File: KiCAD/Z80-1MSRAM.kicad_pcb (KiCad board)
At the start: 2 copper layers, 99.1 x 74.9 mm, 23 parts, among them J1 SBC8080 BUS, U1 7402, U2 74HC573, U3 74HC139, U4 74HC04, U5 74HC00, U6 628128, U7 28C256

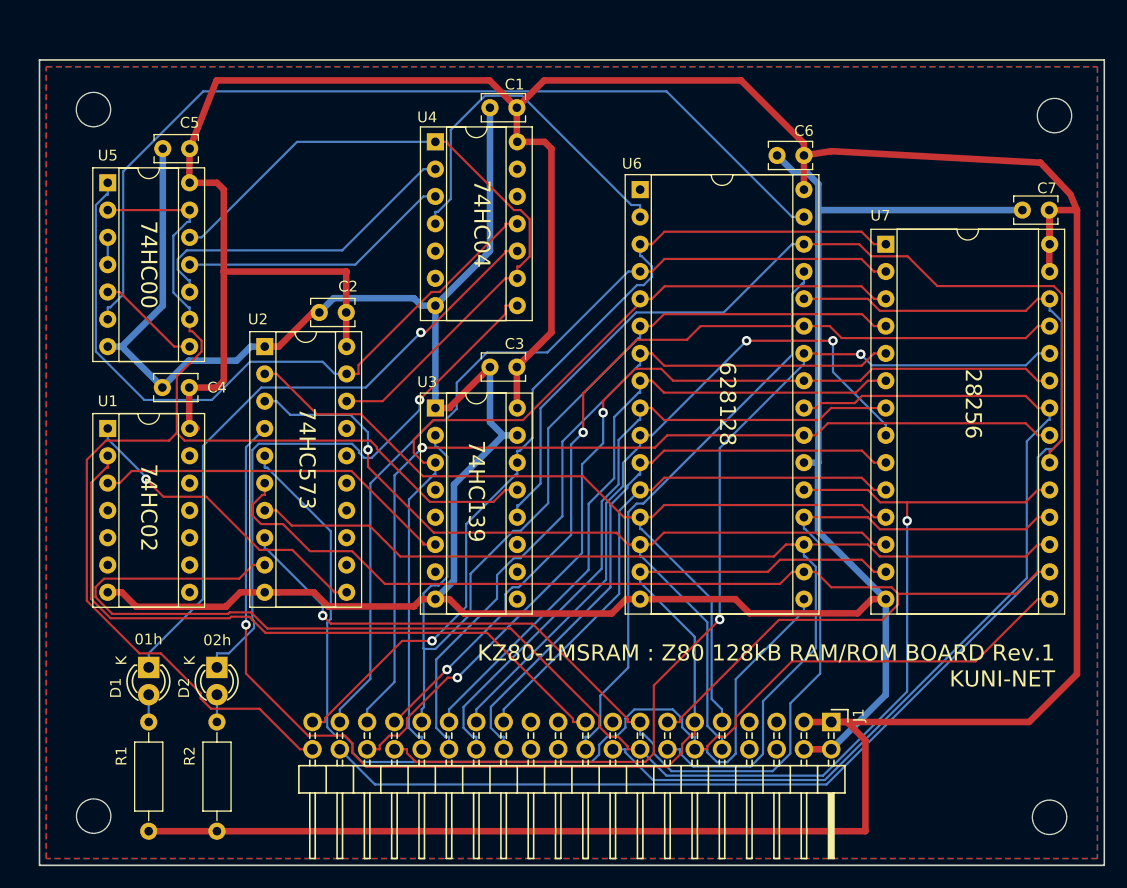
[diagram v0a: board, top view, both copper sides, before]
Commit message: 電源部へコンデンサ追加&パターン調整
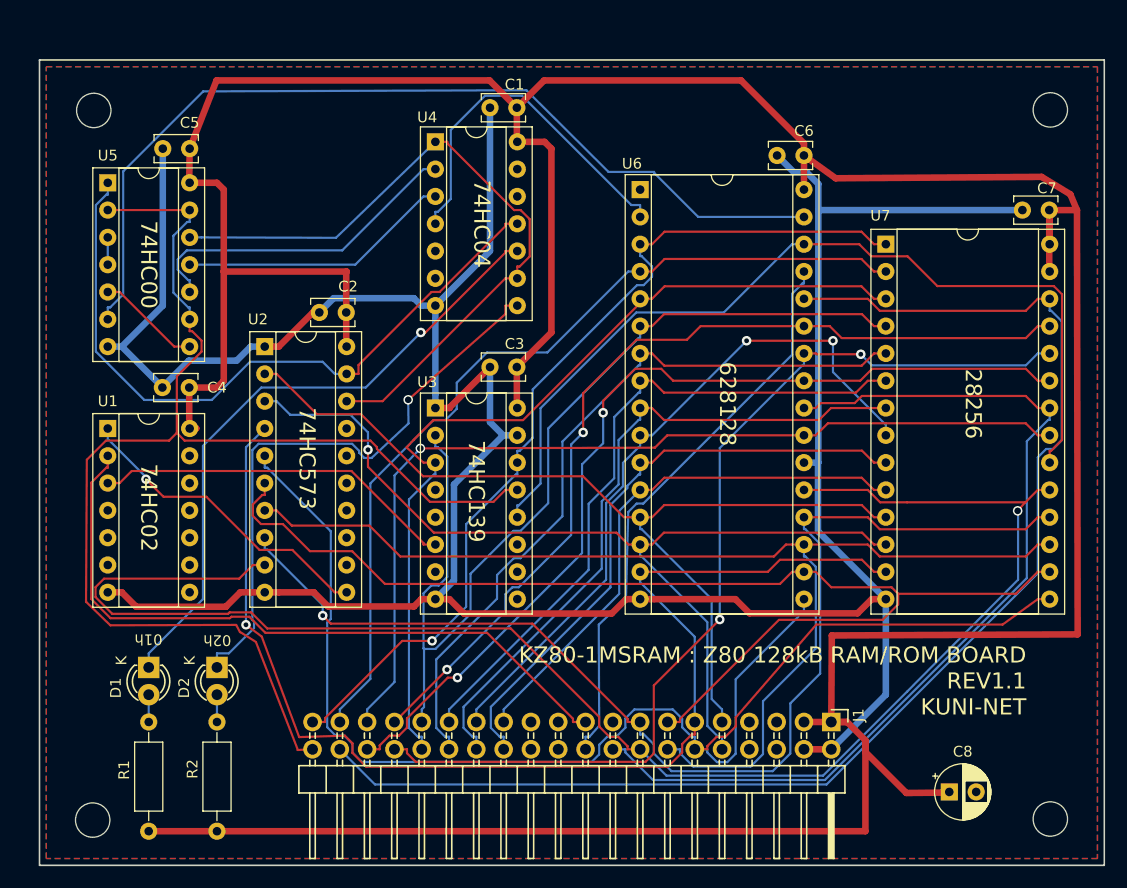
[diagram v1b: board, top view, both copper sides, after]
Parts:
- removed REF** (x4): MountingHole_3.2mm_M3, Mounting_Holes:MountingHole_3.2mm_M3
- added C8: 10u, Capacitor_THT:CP_Radial_D5.0mm_P2.50mm, F.Cu at (186.2, 131.6)
- added MH1: MountingHole, MountingHole:MountingHole_3.2mm_M3, F.Cu at (106.7, 68.2)
- added MH2: MountingHole, MountingHole:MountingHole_3.2mm_M3, F.Cu at (195.6, 68.2)
- added MH3: MountingHole, MountingHole:MountingHole_3.2mm_M3, F.Cu at (106.5, 134.2)
- added MH4: MountingHole, MountingHole:MountingHole_3.2mm_M3, F.Cu at (195.6, 134.1)
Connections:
- J1 pad 17: Net-(J1-Pad17) -> (no net)
- J1 pad 21: Net-(J1-Pad21) -> (no net)
- J1 pad 22: Net-(J1-Pad22) -> (no net)
- J1 pad 23: Net-(J1-Pad23) -> (no net)
- J1 pad 24: Net-(J1-Pad24) -> (no net)
- J1 pad 5: Net-(J1-Pad5) -> (no net)
- J1 pad 6: Net-(J1-Pad6) -> (no net)
- J1 pad 7: Net-(J1-Pad7) -> (no net)
- J1 pad 8: Net-(J1-Pad8) -> (no net)
- U1 pad 10: Net-(U1-Pad10) -> (no net)
- U1 pad 13: Net-(U1-Pad13) -> (no net)
- U1 pad 4: Net-(U1-Pad4) -> (no net)
- U2 pad 12: Net-(U2-Pad12) -> (no net)
- U2 pad 13: Net-(U2-Pad13) -> (no net)
- U2 pad 14: Net-(U2-Pad14) -> (no net)
- U2 pad 15: Net-(U2-Pad15) -> (no net)
- U2 pad 16: Net-(U2-Pad16) -> (no net)
- U2 pad 17: Net-(U2-Pad17) -> (no net)
- U3 pad 10: Net-(U3-Pad10) -> (no net)
- U3 pad 11: Net-(U3-Pad11) -> (no net)
- U3 pad 4: Net-(U3-Pad4) -> (no net)
- U3 pad 5: Net-(U3-Pad5) -> (no net)
- U3 pad 7: Net-(U3-Pad7) -> (no net)
- U3 pad 9: Net-(U3-Pad9) -> (no net)
- U4 pad 12: Net-(U4-Pad12) -> (no net)
- U4 pad 6: Net-(U4-Pad6) -> (no net)
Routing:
- net VCC: track 341.9 -> 356.3 mm
- net /D7: track 145.4 -> 149.9 mm
- net /A15: track 115.8 -> 118.3 mm
- net /A7: track 82.7 -> 83.3 mm
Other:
- board text added: "KZ80-1MSRAM : Z80 128kB RAM/ROM BOARD REV1.1 KUNI-NET"
- board text removed: "KZ80-1MSRAM : Z80 128kB RAM/ROM BOARD Rev.1 KUNI-NET"

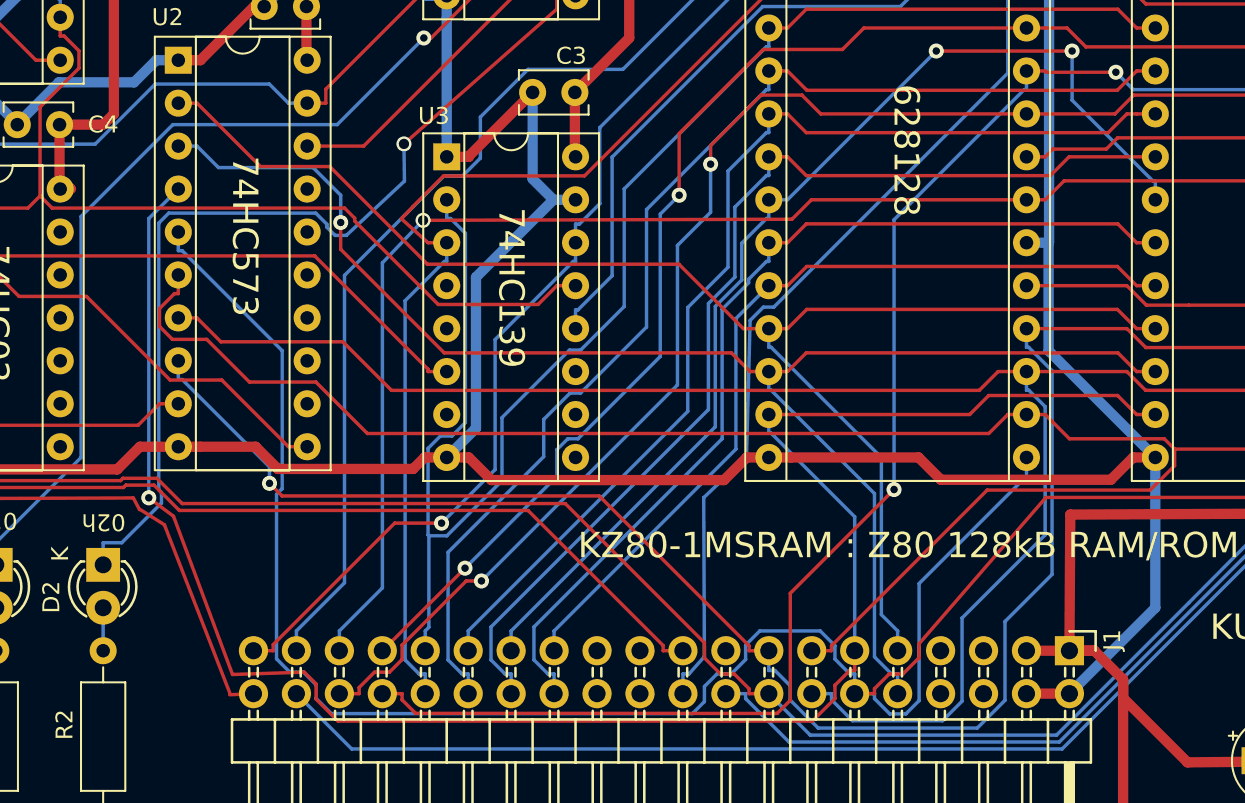
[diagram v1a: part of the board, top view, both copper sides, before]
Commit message: Rev1.1パターン見直し
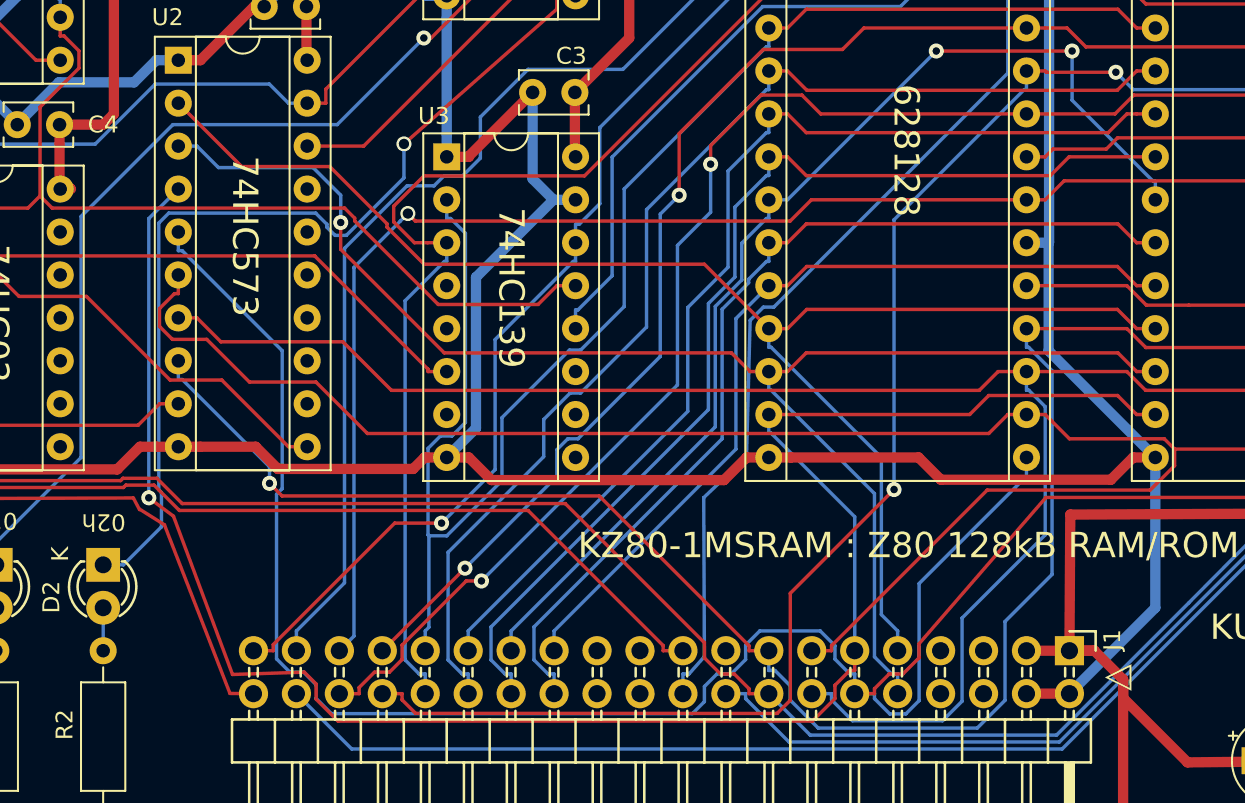
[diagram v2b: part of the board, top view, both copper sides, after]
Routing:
- net /A7: track 83.3 -> 84.8 mm
- net /A10: track 87.4 -> 88.6 mm
- net /A12: track 81.9 -> 82.8 mm
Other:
- board text added: "◁"

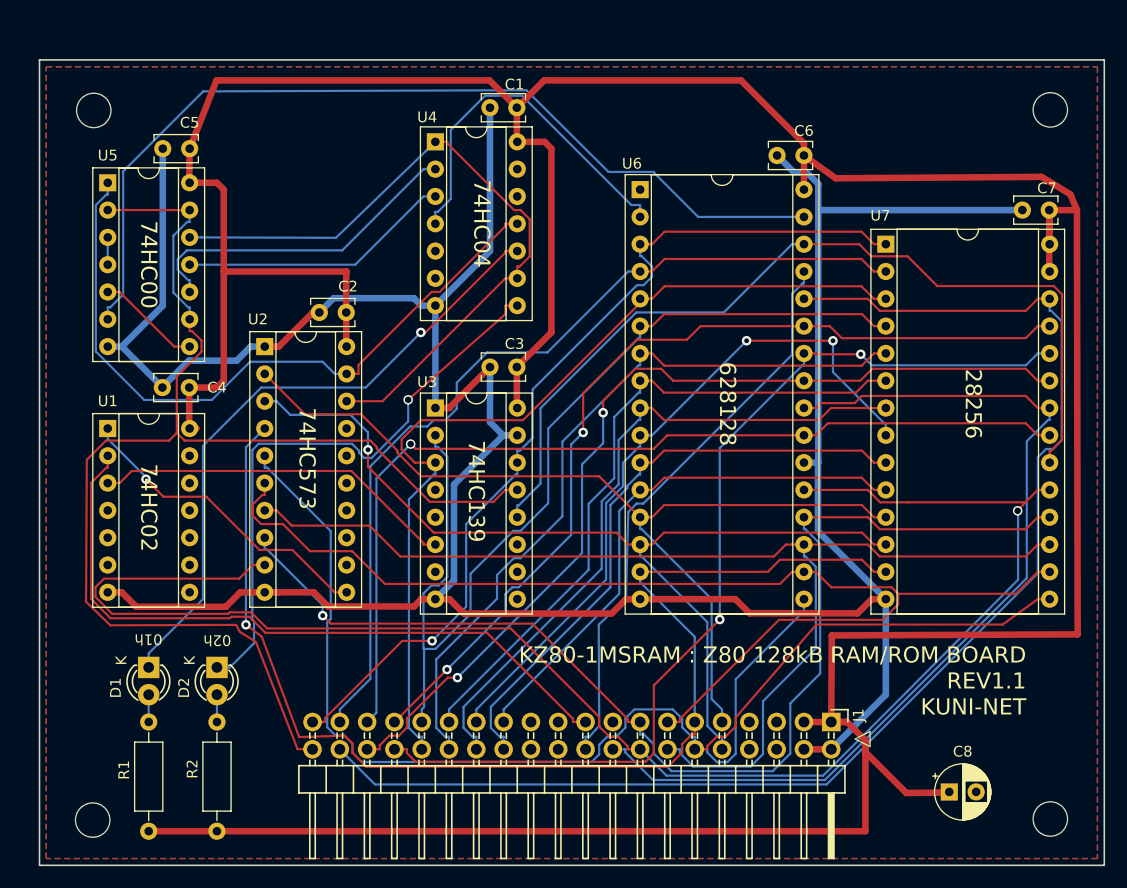
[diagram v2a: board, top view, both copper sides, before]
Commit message: REV2基板対応
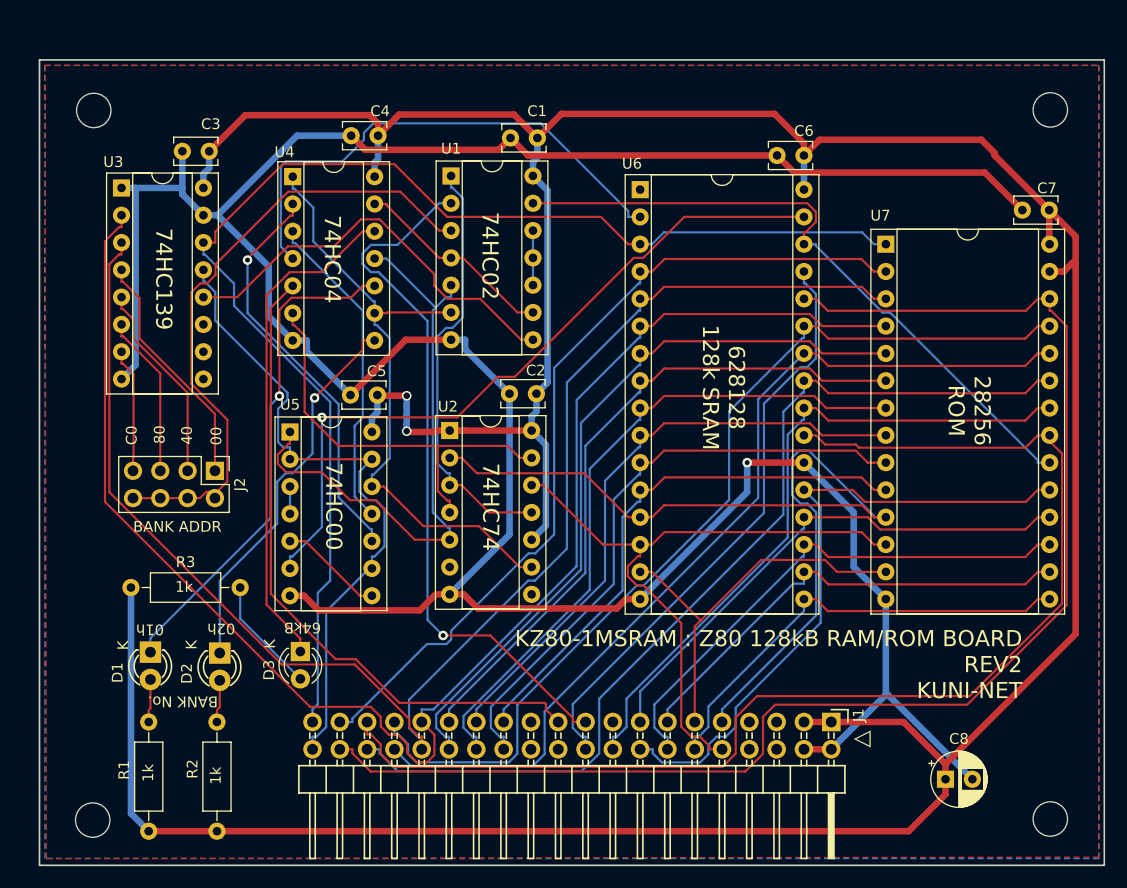
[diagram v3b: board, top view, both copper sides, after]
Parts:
- added D3: LED, LED_THT:LED_D3.0mm, F.Cu at (125.9, 118.5)
- added J2: I/O ADDR SEL, Connector_PinHeader_2.54mm:PinHeader_2x04_P2.54mm_Vertical, F.Cu at (117.9, 101.7)
- added R3: 1k, Resistor_THT:R_Axial_DIN0207_L6.3mm_D2.5mm_P10.16mm_Horizontal, F.Cu at (110.1, 112.6)
- U1: value 7402 -> 74HC02
- U2: value 74HC573 -> 74HC74; footprint Housings_DIP:DIP-20_W7.62mm_Socket -> Package_DIP:DIP-14_W7.62mm_Socket
- moved U1 39.7 mm to (139.9, 74.3)
- moved U3 35.7 mm to (109.2, 75.4)
- moved C3 35.0 mm to (117.4, 72.0)
- moved C4 29.3 mm to (133.1, 70.5)
- moved C5 28.8 mm to (133.0, 94.7)
- moved U5 28.7 mm to (124.9, 98.1)
- moved C2 19.2 mm to (147.8, 94.6)
- moved U2 18.9 mm to (139.8, 98.0)
- moved U4 13.7 mm to (125.2, 74.4)
- moved C1 3.40 mm to (147.9, 70.8)
- moved D1 1.42 mm to (111.9, 118.6)
- moved D2 1.36 mm to (118.4, 118.7)
- moved C8 1.23 mm to (185.9, 130.4)
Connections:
- J1 pad 17: (no net) -> Net-(J1-Pad17)
- J1 pad 21: (no net) -> RES
- J1 pad 22: (no net) -> Net-(J1-Pad22)
- J1 pad 23: (no net) -> Net-(J1-Pad23)
- J1 pad 24: (no net) -> Net-(J1-Pad24)
- J1 pad 5: (no net) -> Net-(J1-Pad5)
- J1 pad 6: (no net) -> Net-(J1-Pad6)
- J1 pad 7: (no net) -> Net-(J1-Pad7)
- J1 pad 8: (no net) -> Net-(J1-Pad8)
- U1 pad 10: (no net) -> Net-(U1-Pad10)
- U1 pad 11: GND -> Net-(U1-Pad10)
- U1 pad 12: GND -> Net-(U1-Pad10)
- U1 pad 13: (no net) -> Net-(U1-Pad13)
- U1 pad 3: /~MSEL -> Net-(J2-Pad2)
- U1 pad 4: (no net) -> Net-(U1-Pad4)
- U1 pad 5: GND -> /DA0
- U1 pad 6: GND -> /DA1
- U1 pad 8: GND -> Net-(U1-Pad8)
- U1 pad 9: GND -> Net-(U1-Pad4)
- U2 pad 1: GND -> VCC
- U2 pad 10: GND -> VCC
- U2 pad 12: (no net) -> /D1
- U2 pad 13: (no net) -> Net-(U2-Pad13)
- U2 pad 14: (no net) -> VCC
- U2 pad 3: /D1 -> Net-(U1-Pad1)
- U2 pad 4: /D2 -> Net-(U2-Pad13)
- U2 pad 5: /D3 -> /DA0
- U2 pad 6: /D4 -> Net-(U2-Pad6)
- U2 pad 7: /D5 -> GND
- U2 pad 8: /D6 -> Net-(U2-Pad8)
- U2 pad 9: /D7 -> /DA1
- U3 pad 10: (no net) -> Net-(U3-Pad10)
- U3 pad 11: (no net) -> Net-(U3-Pad11)
- U3 pad 12: Net-(U3-Pad12) -> Net-(U1-Pad8)
- U3 pad 4: (no net) -> Net-(J2-Pad1)
- U3 pad 5: (no net) -> Net-(J2-Pad3)
- U3 pad 6: /~MSEL -> Net-(J2-Pad5)
- U3 pad 7: (no net) -> Net-(J2-Pad7)
- U3 pad 9: (no net) -> Net-(U3-Pad9)
- U4 pad 12: (no net) -> Net-(D3-Pad1)
- U4 pad 13: GND -> Net-(U1-Pad4)
- U4 pad 5: GND -> RES
- U4 pad 6: (no net) -> Net-(U2-Pad13)
- U6 pad 30: Net-(U3-Pad12) -> Net-(U1-Pad13)
- U7 pad 20: Net-(U3-Pad12) -> Net-(U1-Pad13)
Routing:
- net /D3: track 131.2 -> 42.2 mm
- net /D7: track 149.9 -> 61.2 mm, vias 1 -> 0
- net Net-(U3-Pad12): track 84.1 -> 0.00 mm
- net /D2: track 112.1 -> 37.2 mm, vias 1 -> 0
- net /D4: track 109.7 -> 43.6 mm
- net Net-(U1-Pad13): track 0.00 -> 61.7 mm
- net RES: track 0.00 -> 61.5 mm
- net /D6: track 108.8 -> 49.2 mm, vias 1 -> 0
- net Net-(J2-Pad2): track 0.00 -> 59.1 mm
- net /D5: track 108.5 -> 49.4 mm
- net /A15: track 118.3 -> 62.0 mm
- net /A7: track 84.8 -> 139.7 mm
- net /A6: track 91.9 -> 142.7 mm
- net Net-(D3-Pad1): track 0.00 -> 47.0 mm
- net Net-(U2-Pad13): track 0.00 -> 39.4 mm
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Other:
- board text added: "00"
- board text added: "1k"
- board text added: "28256 ROM"
- board text added: "40"
- board text added: "628128 128k SRAM"
- board text added: "64kB"
- board text added: "74HC74"
- board text added: "80"
- board text added: "BANK ADDR"
- board text added: "BANK No."
- board text added: "C0"
- board text added: "K"
- board text added: "KZ80-1MSRAM : Z80 128kB RAM/ROM BOARD REV2 KUNI-NET"
- board text removed: "28256"
- board text removed: "628128"
- board text removed: "74HC573"
- board text removed: "KZ80-1MSRAM : Z80 128kB RAM/ROM BOARD REV1.1 KUNI-NET"

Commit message: シルクパターン等整備
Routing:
- net GND: vias 1 -> 4
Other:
- board text added: "BANK I/O ADDR"
- board text removed: "BANK ADDR"
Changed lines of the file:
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@@
     (thickness 1.6)
     (drawings 28)
-    (tracks 811)
+    (tracks 814)
     (zones 0)
     (modules 27)
@@
     (pad 1 np_thru_hole circle (at 0 0) (size 3.2 3.2) (drill 3.2) (layers *.Cu *.Mask))
   )
-  (gr_text "BANK ADDR" (at 114.427 106.934) (layer F.SilkS)
+  (gr_text "BANK I/O ADDR" (at 114.427 106.934) (layer F.SilkS)
     (effects (font (size 1 1) (thickness 0.15)))
   )
@@
   (segment (start 124.904 113.3475) (end 126.2123 113.3475) (width 0.6096) (layer F.Cu) (net 6))
   (via (at 167.4345 100.965) (size 0.889) (layers F.Cu B.Cu) (net 6))
+  (via (at 116.205 108.585) (size 0.889) (drill 0.6096) (layers F.Cu B.Cu) (net 6))
+  (via (at 128.27 88.265) (size 0.889) (drill 0.6096) (layers F.Cu B.Cu) (net 6))
+  (via (at 175.26 120.015) (size 0.889) (drill 0.6096) (layers F.Cu B.Cu) (net 6))
   (segment (start 165.1 125.095) (end 165.1 123.9263) (width 0.2032) (layer B.Cu) (net 7))
   (segment (start 180.34 106.045) (end 179.2349 106.045) (width 0.2032) (layer B.Cu) (net 7))

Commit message: REV3 基板関係 試作バージョン
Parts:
- added JP1: A7_Jumper, Connector_PinHeader_2.54mm:PinHeader_1x03_P2.54mm_Vertical, F.Cu at (110.3, 108.0)
- added Q1: 2SC1815, Package_TO_SOT_THT:TO-92L_Inline_Wide, F.Cu at (132.7, 119.7)
- added R4: 100k, Resistor_THT:R_Axial_DIN0207_L6.3mm_D2.5mm_P10.16mm_Horizontal, F.Cu at (141.6, 120.0)
- added R5: 1k, Resistor_THT:R_Axial_DIN0207_L6.3mm_D2.5mm_P10.16mm_Horizontal, F.Cu at (155.6, 120.0)
- R1, R2: footprint Resistors_THT:R_Axial_DIN0207_L6.3mm_D2.5mm_P10.16mm_Horizontal -> Resistor_THT:R_Axial_DIN0207_L6.3mm_D2.5mm_P10.16mm_Horizontal
- moved R1 12.7 mm to (119.9, 125.5), turned to 180 degrees
- moved R2 6.96 mm to (119.9, 128.5), turned to 180 degrees
- moved C8 4.08 mm to (185.4, 126.4)
- moved J2 2.27 mm to (116.9, 99.7)
- moved C1 1.27 mm to (147.9, 69.5)
- moved C2 1.27 mm to (147.8, 93.3)
- moved C4 1.27 mm to (133.1, 69.3)
- moved U2 1.27 mm to (139.8, 96.7)
- moved U4 1.27 mm to (125.2, 73.1)
- moved C5 1.27 mm to (133.0, 93.4)
- moved C6 1.27 mm to (172.7, 71.1)
- moved C7 1.27 mm to (195.5, 76.2)
- moved U1 1.27 mm to (139.9, 73.0)
- moved U5 1.27 mm to (124.9, 96.8)
- moved U6 1.27 mm to (157.5, 74.3)
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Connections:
- J1 pad 32: /A7 -> A7
- U3 pad 1: GND -> ADDR_SEL
- U3 pad 2: /A6 -> /A5
- U3 pad 3: /A7 -> /A6
- U6 pad 5: /A7 -> A7
- U7 pad 3: /A7 -> A7
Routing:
- net /A7: track 139.7 -> 0.00 mm
- net A7: track 0.00 -> 120.1 mm
- net /A5: track 69.3 -> 132.5 mm
- net VCC: track 341.4 -> 281.4 mm, vias 2 -> 0
- net Net-(JP1-Pad1): track 0.00 -> 52.9 mm
- net /A10: track 116.0 -> 80.0 mm, vias 0 -> 1
- net ADDR_SEL: track 0.00 -> 36.0 mm
- net /A13: track 130.1 -> 98.1 mm
- net /A14: track 121.4 -> 151.6 mm
- net /A6: track 142.7 -> 122.3 mm
- net /MEMA16: track 48.4 -> 33.9 mm
- net Net-(J2-Pad2): track 59.1 -> 71.6 mm
- net RES: track 61.5 -> 72.0 mm, vias 0 -> 1
- net /MEMA15: track 68.0 -> 77.4 mm, vias 1 -> 0
- net Net-(D1-Pad1): track 46.6 -> 55.9 mm
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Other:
- net class BOLD: clearance 0.2032 -> 0.2; trace_width 0.6096 -> 0.6; via_dia 0.889 -> 0.8; via_drill 0.6096 -> 0.4
- net class Default: clearance 0.2032 -> 0.2; trace_width 0.2032 -> 0.25; via_dia 0.889 -> 0.8; via_drill 0.6096 -> 0.4
- rule trace_clearance: 0.2032 -> 0.2
- rule trace_min: 0.2032 -> 0.2
- rule via_min_drill: 0.6096 -> 0.4
- rule via_min_size: 0.889 -> 0.8
- board text added: "20"
- board text added: "60"
- board text added: "KZ80-1MSRAM : Z80 128kB RAM/ROM BOARD REV3 KUNI-NET"
- board text removed: "1k"
- board text removed: "C0"
- board text removed: "KZ80-1MSRAM : Z80 128kB RAM/ROM BOARD REV2 KUNI-NET"
